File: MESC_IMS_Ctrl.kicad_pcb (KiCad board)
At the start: 2 copper layers, 100 x 75 mm, 186 parts, among them J1 Conn_01x08_Female, J10 Conn_01x04_Male, J2 Conn_01x08_Female, J3 Conn_01x08_Female, J4 Conn_01x06_Male, J5 Conn_ARM_JTAG_SWD_10, J6 USB_C_Receptacle_USB2.0, J7 Conn_01x03_Male, J8 Conn_01x04_Male, J9 Conn_01x08_Male, U1 STM32F303CBTx, U2 LM5017MR, U3 TPS76333, U4 INA240A1PW, U5 UCC21520DW, U6 INA240A1PW, U7 UCC21520DW, U8 INA240A1PW, U9 UCC21520DW, Y1 ASE-8.000MHZ-LC-T

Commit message: Some more routing
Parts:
- J9: footprint Connector_JST:JST_PH_B8B-PH-SM4-TB_1x08-1MP_P2.00mm_Vertical -> Connector_JST:JST_PH_S8B-PH-SM4-TB_1x08-1MP_P2.00mm_Horizontal
- moved D4 58.9 mm to (155.8, 111.5), turned to 270 degrees
- moved D18 53.5 mm to (153.5, 111.5), turned to 270 degrees
- moved C17 50.5 mm to (225.5, 133.8)
- moved C18 50.5 mm to (222.5, 133.8)
- moved C20 44.9 mm to (225.0, 119.5)
- moved C21 44.9 mm to (222.0, 119.5)
- moved R29 44.9 mm to (223.2, 128.8)
- moved R30 44.9 mm to (223.3, 129.8)
- moved R31 44.9 mm to (227.0, 129.0)
- moved U2 44.9 mm to (223.2, 124.5)
- moved C23 44.3 mm to (213.8, 109.2)
- moved C24 44.3 mm to (214.2, 107.8)
- moved C25 44.3 mm to (226.2, 101.2)
- moved C26 44.3 mm to (220.3, 101.2)
- moved C27 44.3 mm to (226.2, 98.2)
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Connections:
- U7 pad 7: GND -> Net-(U7-Pad7)
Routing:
- net /Phase_U/GATE_DIS: track 68.0 -> 89.9 mm
- net +5V: track 51.0 -> 29.2 mm, vias 3 -> 2
- net /V_SEN: track 0.00 -> 20.9 mm, vias 0 -> 1
- net /U_V_SEN: track 32.4 -> 12.1 mm, vias 2 -> 0
- net /V_V_SEN: track 33.0 -> 13.1 mm, vias 2 -> 0
- net /TMP_INT: track 6.28 -> 22.5 mm
- net /ISU_MCU: track 0.00 -> 14.7 mm
- net +VDC: track 0.00 -> 13.7 mm, vias 0 -> 1
- net /U_I_SEN: track 0.00 -> 13.1 mm
- net /GATE_DIS: track 0.00 -> 11.8 mm, vias 0 -> 2
- net /W_V_SEN: track 0.00 -> 7.35 mm
- net +3V3: track 200.4 -> 194.1 mm
- net /W_I_SEN: track 0.00 -> 5.34 mm
- net /V_I_SEN: track 0.00 -> 5.34 mm
- net /ISW_MCU: track 1.98 -> 7.32 mm
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
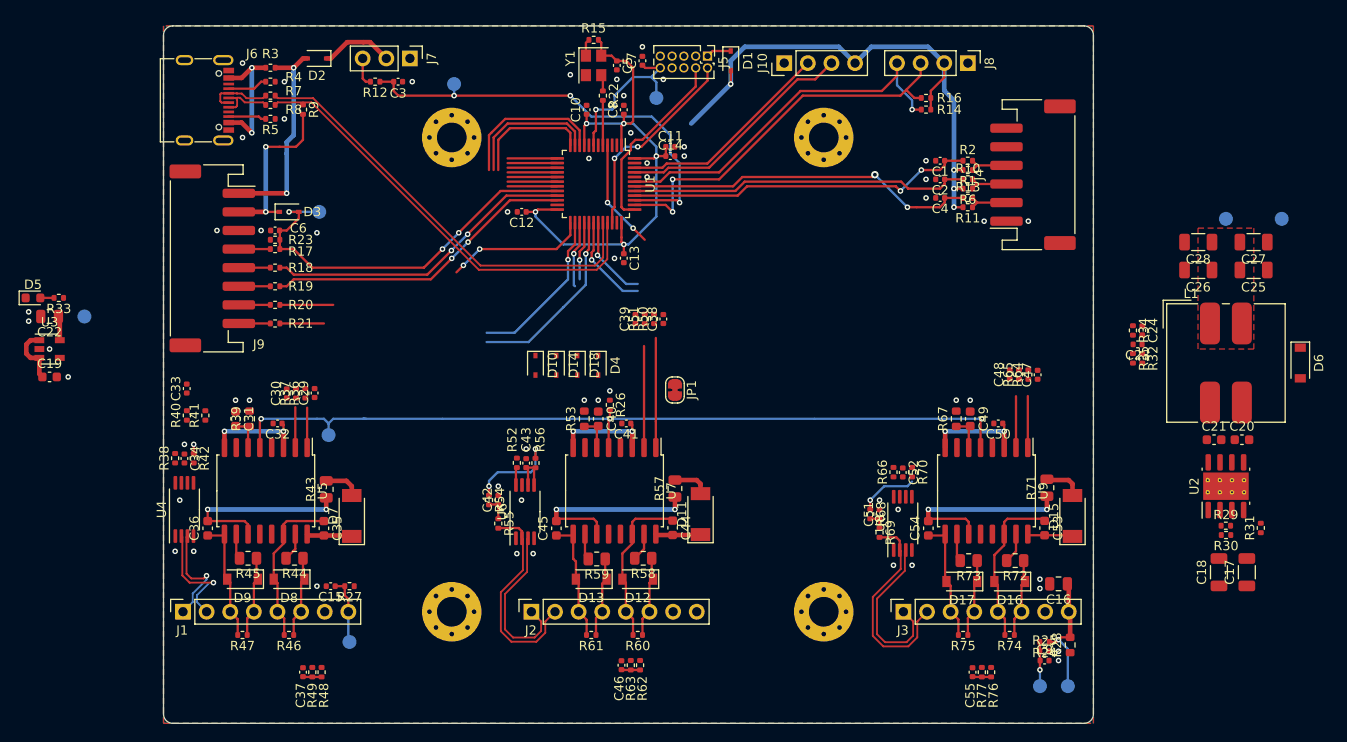
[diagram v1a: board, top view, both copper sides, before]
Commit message: moved crystal, made curr sense regular
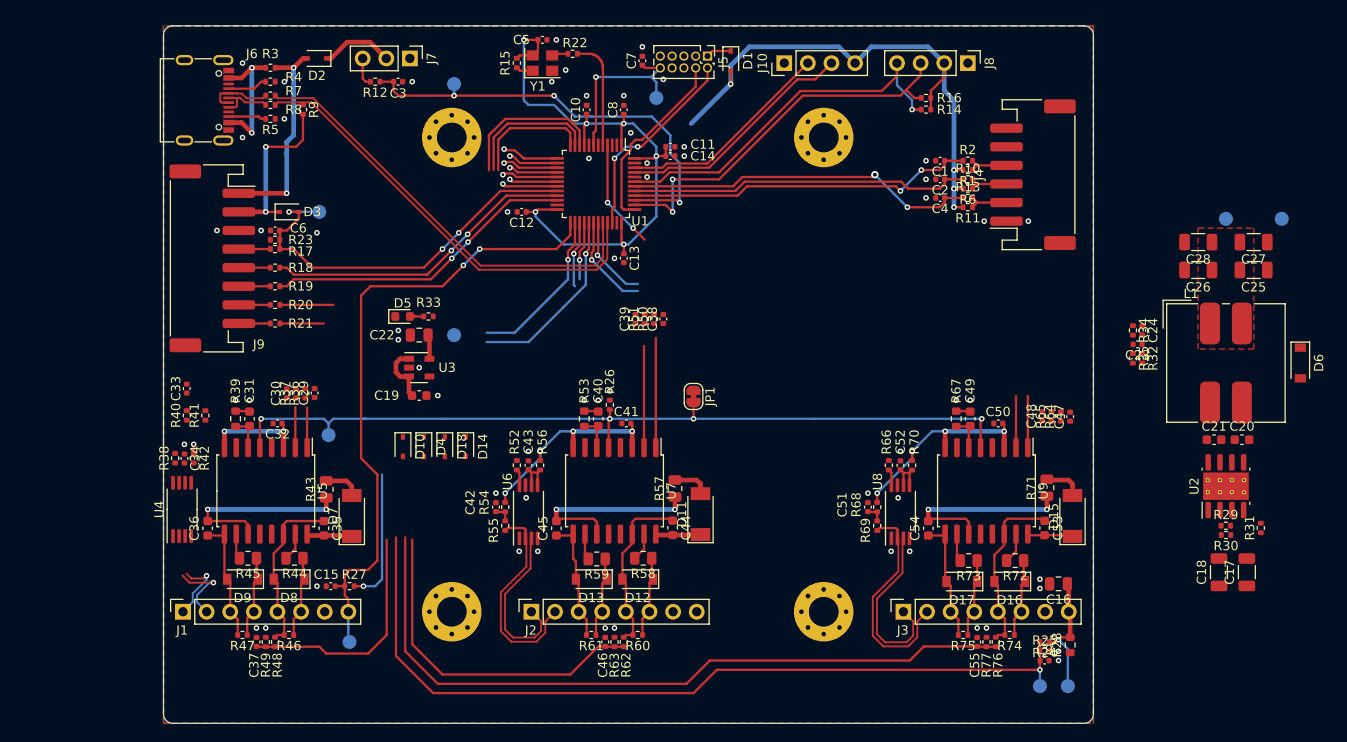
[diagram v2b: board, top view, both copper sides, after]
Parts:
- moved R33 39.8 mm to (137.5, 106.2)
- moved C19 39.8 mm to (136.5, 114.8)
- moved C22 39.8 mm to (136.5, 108.2)
- moved D5 39.8 mm to (134.7, 106.2)
- moved TP8 39.8 mm to (140.2, 108.2), turned to 0 degrees
- moved U3 39.8 mm to (136.5, 111.8)
- moved D4 20.7 mm to (137.0, 120.2)
- moved D10 16.7 mm to (134.8, 120.2)
- moved D18 16.7 mm to (139.2, 120.2)
- moved D14 13.1 mm to (141.5, 120.2)
- moved R15 8.63 mm to (147.0, 79.0), turned to 270 degrees
- moved C5 8.46 mm to (149.8, 76.5), turned to 0 degrees
- moved C37 5.96 mm to (119.0, 141.2)
- moved R48 5.96 mm to (121.0, 141.2)
- moved R49 5.96 mm to (120.0, 141.2)
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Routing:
- net /V_SEN: track 20.9 -> 105.6 mm
- net /W_V_SEN: track 7.35 -> 84.9 mm, vias 0 -> 1
- net /TMP_INT: track 22.5 -> 68.4 mm
- net /V_V_SEN: track 13.1 -> 47.7 mm, vias 0 -> 1
- net +3V3: track 194.1 -> 223.7 mm, vias 21 -> 24
- net /U_V_SEN: track 12.1 -> 36.2 mm, vias 0 -> 1
- net /CLK: track 4.83 -> 11.9 mm
- net GND: track 0.00 -> 4.56 mm, vias 55 -> 61
- net Net-(C52-Pad2): track 0.00 -> 4.20 mm
- net /Phase_U/CURR_SEN-: track 11.5 -> 7.41 mm
- net /Phase_U/CURR_SEN+: track 12.1 -> 8.22 mm
- net /Phase_U/GATE_DIS: track 89.9 -> 91.6 mm, vias 3 -> 4
- net Net-(R66-Pad1): track 0.00 -> 1.74 mm
- net /~RESET: track 18.1 -> 19.4 mm
- net /Phase_W/CURR_SEN-: track 17.9 -> 19.0 mm
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
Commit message: Tweaked LM5017 package
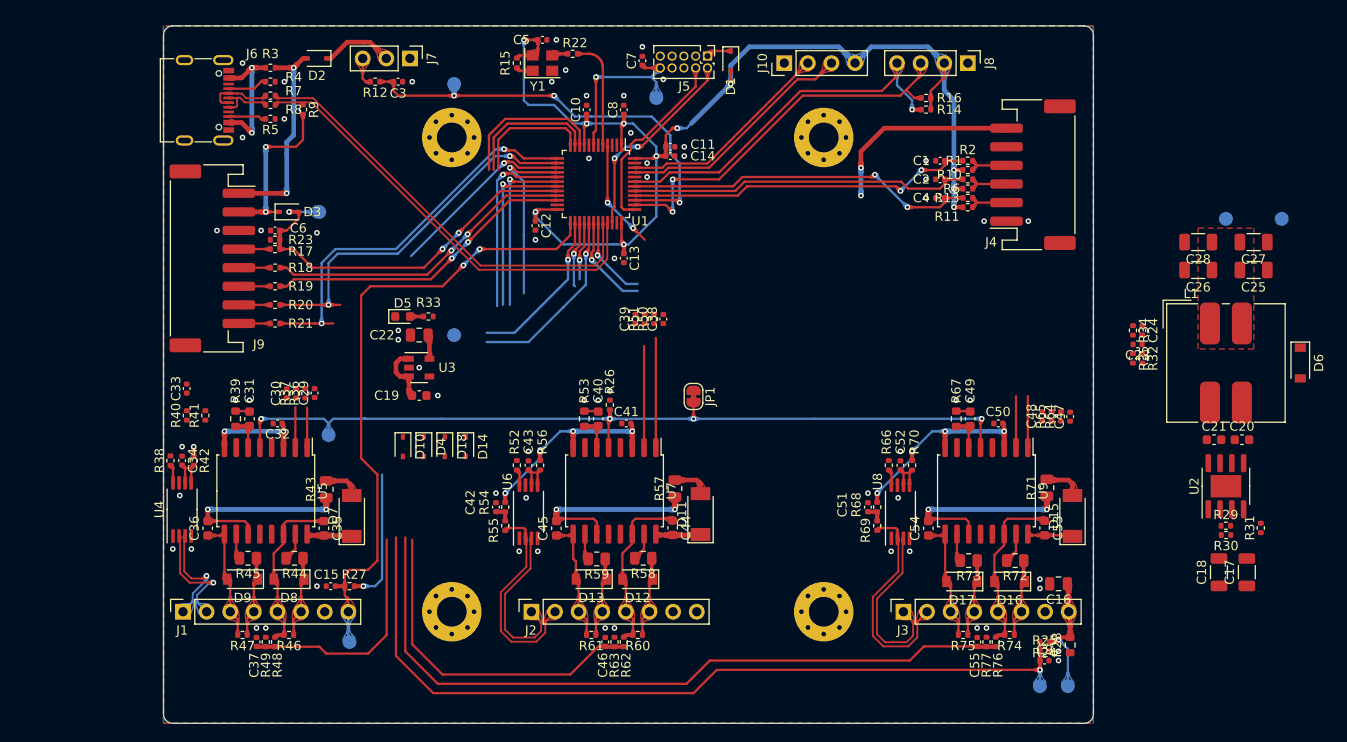
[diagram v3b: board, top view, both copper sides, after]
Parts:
- U2: footprint Package_SO:SOIC-8-1EP_3.9x4.9mm_P1.27mm_EP2.95x4.9mm_Mask2.71x3.4mm_ThermalVias -> Package_SO:SOIC-8-1EP_3.9x4.9mm_P1.27mm_EP2.41x3.3mm
- moved C12 2.09 mm to (149.0, 96.5), turned to 270 degrees
- moved R38 0.56 mm to (109.8, 121.8)
- moved C34 0.34 mm to (111.0, 121.8)
- moved R42 0.26 mm to (112.2, 121.8)
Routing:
- net /U_V_SEN: track 36.2 -> 68.4 mm, vias 1 -> 2
- net /V_V_SEN: track 47.7 -> 77.3 mm, vias 1 -> 2
- net +5V: track 29.2 -> 50.6 mm, vias 2 -> 4
- net /ISV_MCU: track 8.04 -> 22.4 mm
- net /W_V_SEN: track 84.9 -> 99.0 mm
- net /V_I_SEN: track 5.29 -> 19.4 mm
- net /ISW_MCU: track 7.18 -> 20.7 mm
- net /W_I_SEN: track 5.94 -> 18.9 mm
- net Net-(C34-Pad2): track 0.00 -> 4.69 mm
- net +3V3: track 223.7 -> 228.2 mm, vias 24 -> 25
- net /Phase_U/CURR_SEN+: track 8.22 -> 12.6 mm
- net /Phase_U/CURR_SEN-: track 7.41 -> 11.6 mm
- net Net-(R38-Pad1): track 0.00 -> 1.99 mm
- net GND: vias 61 -> 64

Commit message: Removed coupled inductor
Added TPS61041DB
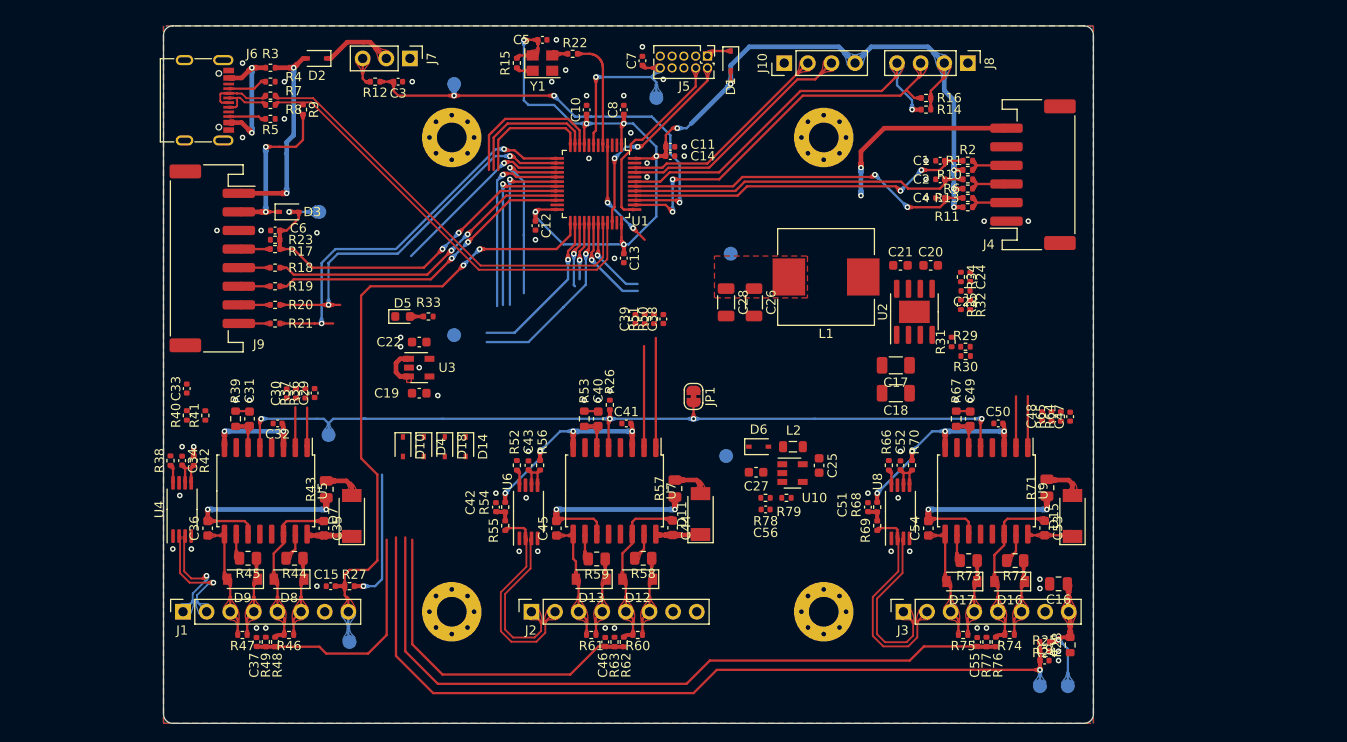
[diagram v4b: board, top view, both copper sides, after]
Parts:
- added C56: 10pF, Capacitor_SMD:C_0402_1005Metric, F.Cu at (173.8, 127.0)
- added L2: 10uH 0.5A, Inductor_SMD:L_0805_2012Metric, F.Cu at (176.7, 120.2)
- added R78: 2M, Resistor_SMD:R_0402_1005Metric, F.Cu at (173.7, 125.8)
- added R79: 180k, Resistor_SMD:R_0402_1005Metric, F.Cu at (176.0, 125.8)
- added U10: TPS61041DBV, Package_TO_SOT_SMD:SOT-23-5, F.Cu at (176.6, 123.1)
- C22: value 4.7uF 6.3V -> 4.7uF 16V; footprint Capacitor_SMD:C_0805_2012Metric -> Capacitor_SMD:C_0603_1608Metric
- C25: value 10uF -> 4.7uF 16V; footprint Capacitor_SMD:C_1206_3216Metric -> Capacitor_SMD:C_0603_1608Metric
- C27: value 10uF -> 1uF 50V; footprint Capacitor_SMD:C_1206_3216Metric -> Capacitor_SMD:C_0603_1608Metric
- D6: value MBR130 -> D; footprint Diode_SMD:D_SOD-123 -> Diode_SMD:D_SOD-323
- L1: value SRF1260-101M -> 100uH 1.5A; footprint Inductor_SMD:L_Bourns_SRF1260 -> Inductor_SMD:L_Wuerth_HCI-1040
- moved TP9 65.0 mm to (169.5, 121.2), turned to 0 degrees
- moved C27 58.9 mm to (172.7, 123.0), turned to 0 degrees
- moved D6 58.9 mm to (173.0, 120.2), turned to 0 degrees
- moved TP10 53.4 mm to (170.0, 99.5), turned to 0 degrees
- moved C25 51.2 mm to (179.5, 122.3), turned to 270 degrees
- moved C28 51.2 mm to (169.5, 104.7), turned to 270 degrees
- moved C26 47.9 mm to (172.5, 104.7), turned to 270 degrees
- moved L1 44.0 mm to (180.2, 102.0), turned to 180 degrees
- moved C17 43.8 mm to (187.8, 111.5), turned to 180 degrees
- moved C18 39.7 mm to (187.8, 114.5), turned to 180 degrees
- moved R31 38.8 mm to (193.8, 109.0)
- moved C21 38.6 mm to (188.2, 100.8)
- moved U2 38.4 mm to (189.8, 105.8)
- moved C20 38.4 mm to (191.5, 100.8)
- moved R29 34.0 mm to (195.2, 109.5)
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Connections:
- C25 pad 1: VDD -> +5V
- C25 pad 2: +5V -> GND
- C27 pad 2: +5V -> GND
- L1 pad 1: +5V -> Net-(C21-Pad1)
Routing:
- net +3V3: track 228.2 -> 225.6 mm
- net +5V: track 50.6 -> 48.4 mm

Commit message: Playing with pours
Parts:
- moved R29 4.74 mm to (190.8, 111.0), turned to 90 degrees
- moved R31 2.67 mm to (192.0, 111.0)
- moved C56 2.55 mm to (173.3, 124.5)
- moved R30 2.07 mm to (193.2, 111.0), turned to 270 degrees
- moved TP10 1.52 mm to (171.5, 99.8)
- moved C18 1.00 mm to (187.8, 113.5)
- moved R79 0.74 mm to (175.2, 125.8)
- moved C17 0.50 mm to (187.8, 111.0)
- moved C27 0.50 mm to (172.7, 122.5)
- moved R78 0.49 mm to (173.2, 125.8)
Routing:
- net +5V: track 48.4 -> 54.4 mm, vias 4 -> 7
- net Net-(C56-Pad2): track 0.00 -> 4.21 mm
- net VDD: track 63.0 -> 66.6 mm
- net Net-(C20-Pad1): track 0.00 -> 2.67 mm
- net Net-(C21-Pad2): track 0.00 -> 2.56 mm
- net GND: vias 64 -> 86
- added copper zone on F.Cu, net Net-(C17-Pad1)
- added copper zone on F.Cu, net Net-(C21-Pad1)
- added copper zone on F.Cu, net Net-(D6-Pad2)
- added copper zone on F.Cu, net VDD

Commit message: Some minor tweaks
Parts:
- moved R32 10.5 mm to (186.8, 99.5), turned to 180 degrees
- moved R35 10.3 mm to (186.8, 98.5), turned to 180 degrees
- moved C23 8.32 mm to (188.2, 99.0), turned to 90 degrees
- moved C24 6.50 mm to (189.8, 99.5), turned to 180 degrees
- moved R34 6.10 mm to (189.8, 98.5), turned to 180 degrees
- moved R30 2.79 mm to (190.5, 111.5)
- moved C17 1.58 mm to (186.2, 111.5)
- moved C18 1.58 mm to (186.3, 114.0)
- moved C20 1.58 mm to (190.0, 101.2)
- moved C21 1.58 mm to (186.8, 101.2)
- moved C26 1.58 mm to (171.0, 105.2)
- moved C28 1.58 mm to (168.0, 105.2)
- moved L1 1.58 mm to (178.8, 102.5)
- moved R29 1.58 mm to (189.2, 111.5)
- moved TP10 1.58 mm to (170.0, 100.2)
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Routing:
- net +5V: track 54.4 -> 77.1 mm, vias 7 -> 9
- net Net-(C23-Pad2): track 0.00 -> 15.5 mm, vias 0 -> 2
- net Net-(C17-Pad1): track 0.00 -> 7.31 mm
- net Net-(R29-Pad2): track 0.00 -> 3.68 mm
- net Net-(R31-Pad2): track 0.00 -> 3.40 mm
- net Net-(C23-Pad1): track 0.00 -> 2.03 mm
- net Net-(C21-Pad1): track 0.00 -> 1.86 mm
- net GND: vias 86 -> 85

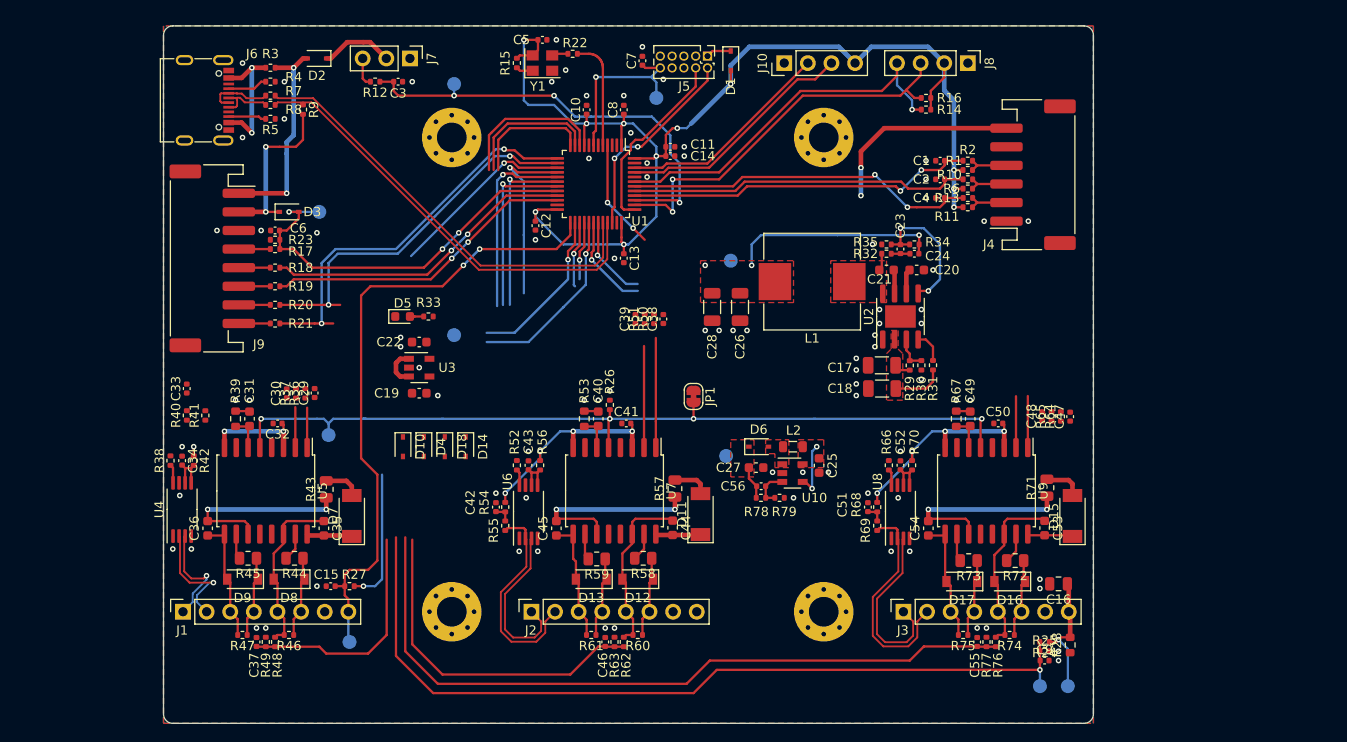
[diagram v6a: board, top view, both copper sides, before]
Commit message: Tweaking potential dividers
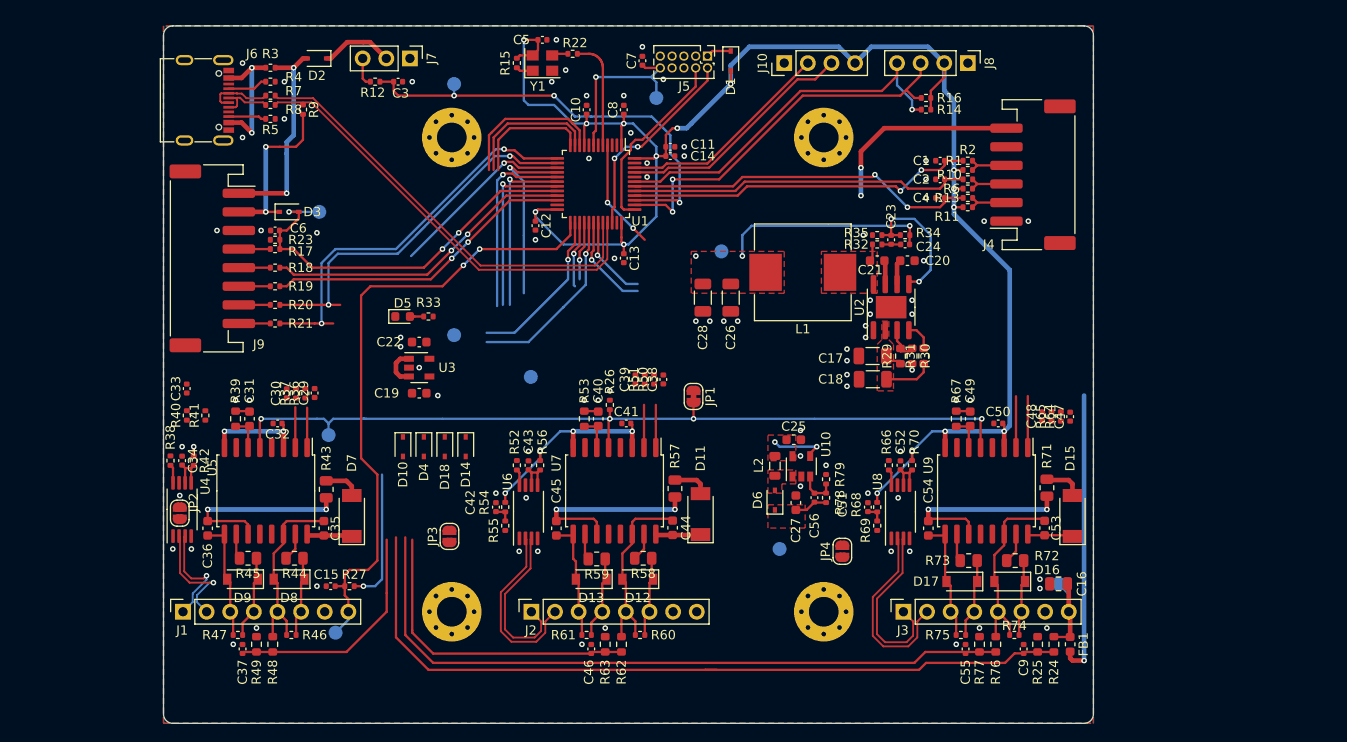
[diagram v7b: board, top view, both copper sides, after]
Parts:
- removed R28: 10R, Resistor_SMD:R_0603_1608Metric
- added FB1: 0R1, Inductor_SMD:L_0603_1608Metric, F.Cu at (206.5, 141.5)
- added JP2: SolderJumper_2_Open, Jumper:SolderJumper-2_P1.3mm_Open_RoundedPad1.0x1.5mm, F.Cu at (110.8, 127.4)
- added JP3: SolderJumper_2_Open, Jumper:SolderJumper-2_P1.3mm_Open_RoundedPad1.0x1.5mm, F.Cu at (139.8, 129.9)
- added JP4: SolderJumper_2_Open, Jumper:SolderJumper-2_P1.3mm_Open_RoundedPad1.0x1.5mm, F.Cu at (182.0, 131.5)
- R24, R25, R29, R30, R31, R48, R49, R62, R63, R76, R77: footprint Resistor_SMD:R_0402_1005Metric -> Resistor_SMD:R_0603_1608Metric
- moved TP2 64.1 mm to (148.5, 112.8)
- moved TP9 11.5 mm to (175.2, 131.2)
- moved TP7 11.0 mm to (205.2, 135.0)
- moved R78 7.00 mm to (180.2, 125.8), turned to 90 degrees
- moved C38 6.50 mm to (162.8, 113.0)
- moved C39 6.50 mm to (159.8, 113.0)
- moved R50 6.50 mm to (161.8, 113.0)
- moved R51 6.50 mm to (160.8, 113.0)
- moved D6 6.01 mm to (174.8, 126.0), turned to 90 degrees
- moved C56 5.86 mm to (179.0, 125.7), turned to 90 degrees
- moved C27 5.70 mm to (177.0, 126.3), turned to 90 degrees
- moved R79 5.39 mm to (180.2, 123.8), turned to 90 degrees
- moved C25 3.89 mm to (176.8, 119.5), turned to 0 degrees
- moved L2 2.83 mm to (174.8, 122.3), turned to 270 degrees
- moved C9 2.57 mm to (201.5, 142.0), turned to 90 degrees
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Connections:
- net Net-(C17-Pad1) renamed /PSUs/VCC
- R41 pad 2: /Phase_U/CURR_SEN+ -> Net-(JP2-Pad2)
- R55 pad 2: /Phase_V/CURR_SEN+ -> Net-(JP3-Pad2)
- R69 pad 2: /Phase_W/CURR_SEN+ -> Net-(JP4-Pad2)
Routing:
- net /PSUs/VCC: track 7.31 -> 38.1 mm, vias 0 -> 1
- net +3V3: track 225.6 -> 252.5 mm
- net Net-(C38-Pad1): track 11.8 -> 4.60 mm
- net Net-(C39-Pad1): track 10.9 -> 4.60 mm
- net /V_SEN: track 105.6 -> 101.3 mm, vias 1 -> 0
- net /Phase_W/CURR_SEN+: track 23.8 -> 20.5 mm
- net /Phase_V/CURR_SEN+: track 22.8 -> 19.5 mm
- net /V_V_SEN: track 77.3 -> 74.2 mm
- net /W_V_SEN: track 99.0 -> 96.0 mm
- net +VDC: track 13.7 -> 11.1 mm, vias 1 -> 0
- net /Phase_U/G_MID: track 18.4 -> 20.3 mm
- net /Phase_W/G_MID: track 18.7 -> 20.6 mm
- net /Phase_V/G_MID: track 18.7 -> 20.6 mm
- net GND: vias 85 -> 84
